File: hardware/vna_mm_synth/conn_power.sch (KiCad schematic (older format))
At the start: 19 parts, among them J201 Conn_02x10_Odd_Even, J202 Conn_Coaxial, U201 74HC244, U202 LM71CIMF

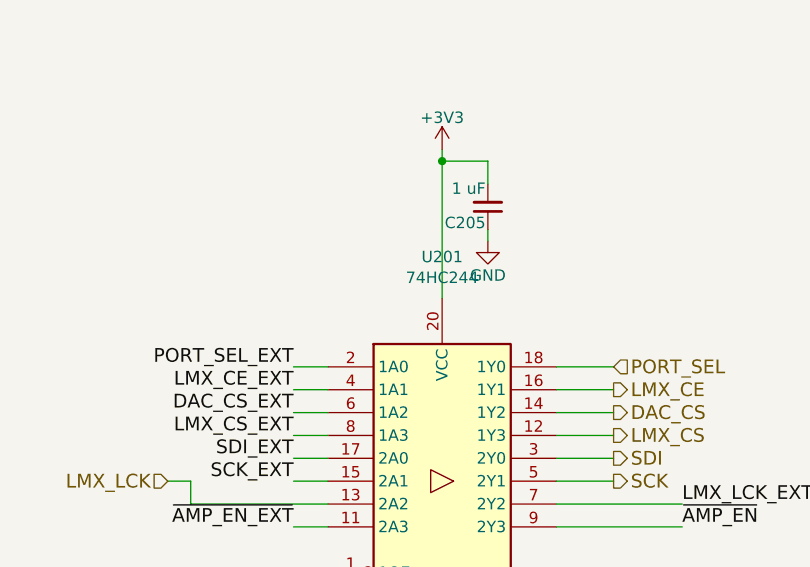
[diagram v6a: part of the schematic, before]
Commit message: footprint assignment on vna_mm_synth
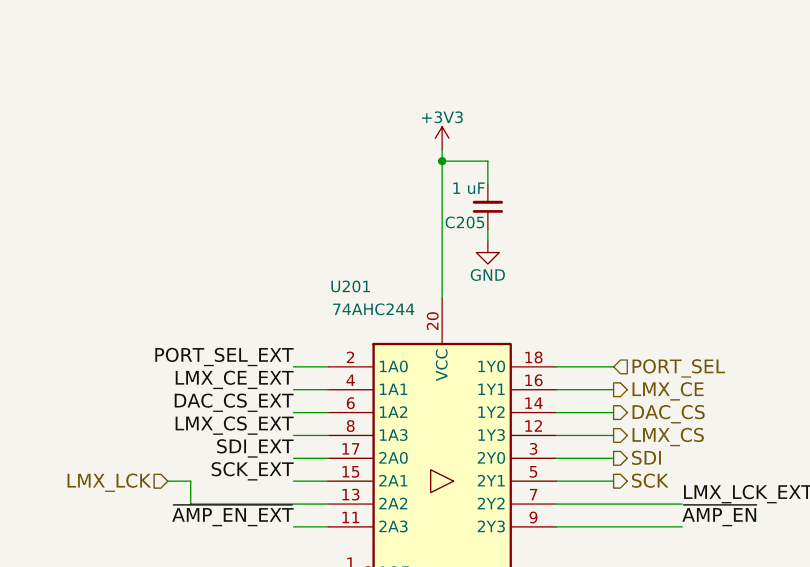
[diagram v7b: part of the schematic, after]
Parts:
- U201: value 74HC244 -> 74AHC244; footprint (none) -> Package_SO:TSSOP-20_4.4x6.5mm_P0.65mm
- U202: footprint TO_SOT_Packages_SMD:SOT-23-5 -> Package_TO_SOT_SMD:SOT-23-5
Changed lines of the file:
@@
 EESchema Schematic File Version 4
-LIBS:vna_mm_synth-cache
 EELAYER 30 0
 EELAYER END
@@
 F 0 "U202" H 8728 3296 50  0000 L CNN
 F 1 "LM71CIMF" H 8728 3205 50  0000 L CNN
-F 2 "TO_SOT_Packages_SMD:SOT-23-5" H 7700 3800 50  0001 C CNN
+F 2 "Package_TO_SOT_SMD:SOT-23-5" H 7700 3800 50  0001 C CNN
 F 3 "http://www.ti.com/lit/ds/symlink/lm71.pdf" H 8150 3350 50  0001 C CNN
 	1    8550 3250
@@
 U 1 1 5DF0D107
 P 7750 6650
-F 0 "U201" H 7750 7631 50  0000 C CNN
-F 1 "74HC244" H 7750 7540 50  0000 C CNN
-F 2 "" H 7750 6650 50  0001 C CNN
+F 0 "U201" H 7350 7500 50  0000 C CNN
+F 1 "74AHC244" H 7450 7400 50  0000 C CNN
+F 2 "Package_SO:TSSOP-20_4.4x6.5mm_P0.65mm" H 7750 6650 50  0001 C CNN
 F 3 "https://assets.nexperia.com/documents/data-sheet/74HC_HCT244.pdf" H 7750 6650 50  0001 C CNN
 	1    7750 6650

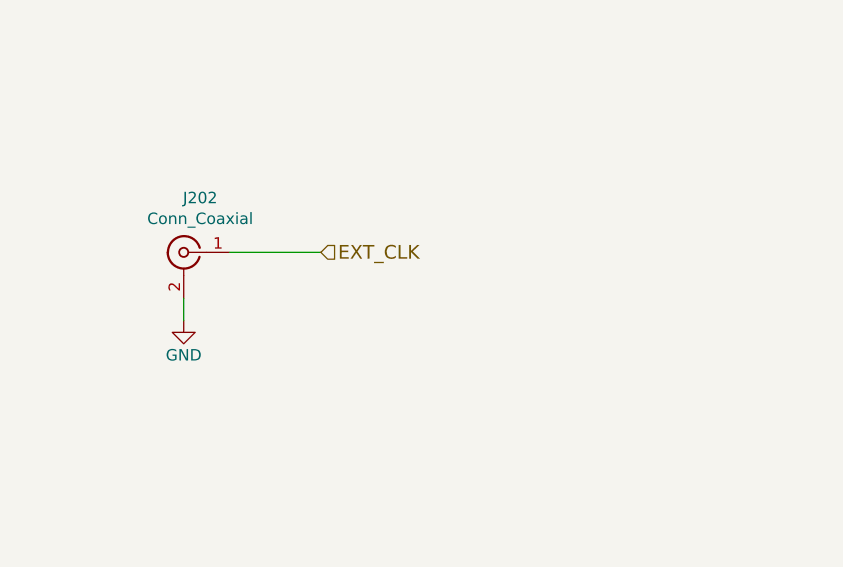
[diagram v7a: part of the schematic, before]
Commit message: added power input protection, footprint assignment on synth
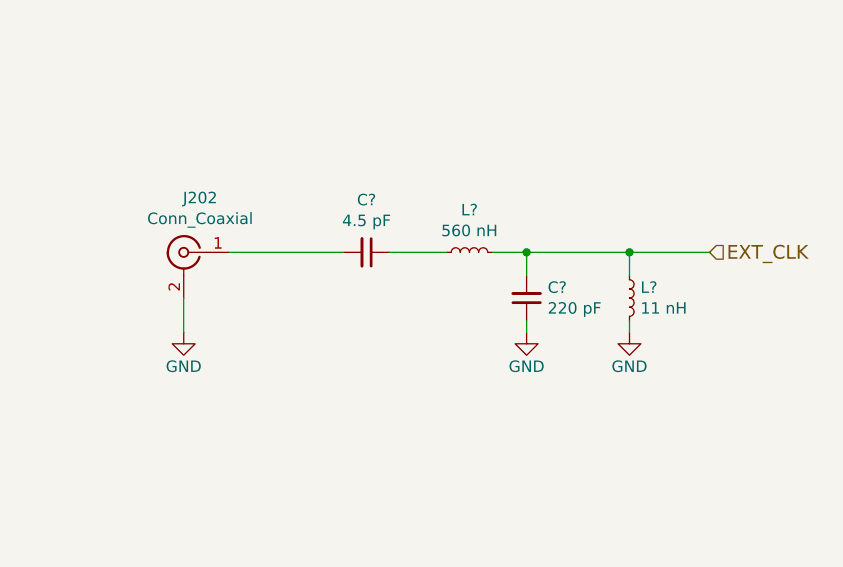
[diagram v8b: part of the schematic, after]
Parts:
- added C?: 4.5 pF, symbol Device:C_Small
- added C?: 220 pF, symbol Device:C_Small
- added L?: 560 nH, symbol Device:L_Small
- added L?: 11 nH, symbol Device:L_Small
- J201: footprint (none) -> Connector_PinHeader_2.54mm:PinHeader_2x10_P2.54mm_Vertical_SMD
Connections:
- net EXT_CLK: now also C?.2, L?.1, L?.2; no longer J202.1 (In)
- net GND: now also C?.1, L?.2
- new net: C?.1, L?.1
- new net: C?.2, J202.1 (In)
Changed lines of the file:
@@
 $Descr A3 16535 11693
 encoding utf-8
-Sheet 2 11
+Sheet 2 12
 Title ""
 Date ""
@@
 L power:GND #PWR0227
 U 1 1 5AB94674
-P 10500 6550
-F 0 "#PWR0227" H 10500 6300 50  0001 C CNN
-F 1 "GND" H 10500 6400 50  0000 C CNN
-F 2 "" H 10500 6550 50  0001 C CNN
-F 3 "" H 10500 6550 50  0001 C CNN
-	1    10500 6550
-	1    0    0    -1
-$EndComp
-Text HLabel 11100 6250 2    60   Input ~ 0
+P 10500 6600
+F 0 "#PWR0227" H 10500 6350 50  0001 C CNN
+F 1 "GND" H 10500 6450 50  0000 C CNN
+F 2 "" H 10500 6600 50  0001 C CNN
+F 3 "" H 10500 6600 50  0001 C CNN
+	1    10500 6600
+	1    0    0    -1
+$EndComp
+Text HLabel 12800 6250 2    60   Input ~ 0
 EXT_CLK
 Text Label 4550 6250 0    60   ~ 0
@@
 ~AMP_EN_EXT
 Wire Wire Line
-	11100 6250 10700 6250
-Wire Wire Line
 	8250 6150 8500 6150
 Wire Wire Line
@@
 F 0 "J201" H 4150 6767 50  0000 C CNN
 F 1 "Conn_02x10_Odd_Even" H 4150 6676 50  0000 C CNN
-F 2 "" H 4100 6150 50  0001 C CNN
+F 2 "Connector_PinHeader_2.54mm:PinHeader_2x10_P2.54mm_Vertical_SMD" H 4100 6150 50  0001 C CNN
 F 3 "~" H 4100 6150 50  0001 C CNN
 	1    4100 6150
@@
 	-1   0    0    -1
 $EndComp
-Wire Wire Line
-	10500 6450 10500 6550
+$Comp
+L Device:L_Small L?
+U 1 1 5DEE4A24
+P 11750 6250
+F 0 "L?" V 11935 6250 50  0000 C CNN
+F 1 "560 nH" V 11844 6250 50  0000 C CNN
+F 2 "" H 11750 6250 50  0001 C CNN
+F 3 "~" H 11750 6250 50  0001 C CNN
+	1    11750 6250
+	0    -1   -1   0
+$EndComp
+$Comp
+L Device:C_Small C?
+U 1 1 5DEE5860
+P 11300 6250
+F 0 "C?" V 11071 6250 50  0000 C CNN
+F 1 "4.5 pF" V 11162 6250 50  0000 C CNN
+F 2 "" H 11300 6250 50  0001 C CNN
+F 3 "~" H 11300 6250 50  0001 C CNN
+	1    11300 6250
+	0    1    1    0
+$EndComp
+Wire Wire Line
+	10700 6250 11200 6250
+Wire Wire Line
+	11400 6250 11650 6250
+$Comp
+L Device:C_Small C?
+U 1 1 5DEF252B
+P 12000 6450
+F 0 "C?" H 11908 6404 50  0000 R CNN
+F 1 "220 pF" H 11908 6495 50  0000 R CNN
+F 2 "" H 12000 6450 50  0001 C CNN
+F 3 "~" H 12000 6450 50  0001 C CNN
+	1    12000 6450
+	-1   0    0    1
+$EndComp
+$Comp
+L Device:L_Small L?
+U 1 1 5DEF2945
+P 12450 6450
+F 0 "L?" H 12498 6496 50  0000 L CNN
+F 1 "11 nH" H 12498 6405 50  0000 L CNN
+F 2 "" H 12450 6450 50  0001 C CNN
+F 3 "~" H 12450 6450 50  0001 C CNN
+	1    12450 6450
+	1    0    0    -1
+$EndComp
+$Comp
+L power:GND #PWR?
+U 1 1 5DEF4D1D
+P 12000 6600
+F 0 "#PWR?" H 12000 6350 50  0001 C CNN
+F 1 "GND" H 12000 6450 50  0000 C CNN
+F 2 "" H 12000 6600 50  0001 C CNN
+F 3 "" H 12000 6600 50  0001 C CNN
+	1    12000 6600
+	1    0    0    -1
+$EndComp
+$Comp
+L power:GND #PWR?
+U 1 1 5DEF5155
+P 12450 6600
+F 0 "#PWR?" H 12450 6350 50  0001 C CNN
+F 1 "GND" H 12450 6450 50  0000 C CNN
+F 2 "" H 12450 6600 50  0001 C CNN
+F 3 "" H 12450 6600 50  0001 C CNN
+	1    12450 6600
+	1    0    0    -1
+$EndComp
+Wire Wire Line
+	10500 6450 10500 6600
+Wire Wire Line
+	11850 6250 12000 6250
+Wire Wire Line
+	12000 6250 12000 6350
+Wire Wire Line
+	12000 6250 12450 6250
+Wire Wire Line
+	12450 6250 12450 6350
+Connection ~ 12000 6250
+Wire Wire Line
+	12450 6250 12800 6250
+Connection ~ 12450 6250
+Wire Wire Line
+	12450 6550 12450 6600
+Wire Wire Line
+	12000 6550 12000 6600
 $EndSCHEMATC
